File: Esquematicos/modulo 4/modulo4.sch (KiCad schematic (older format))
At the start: 15 parts

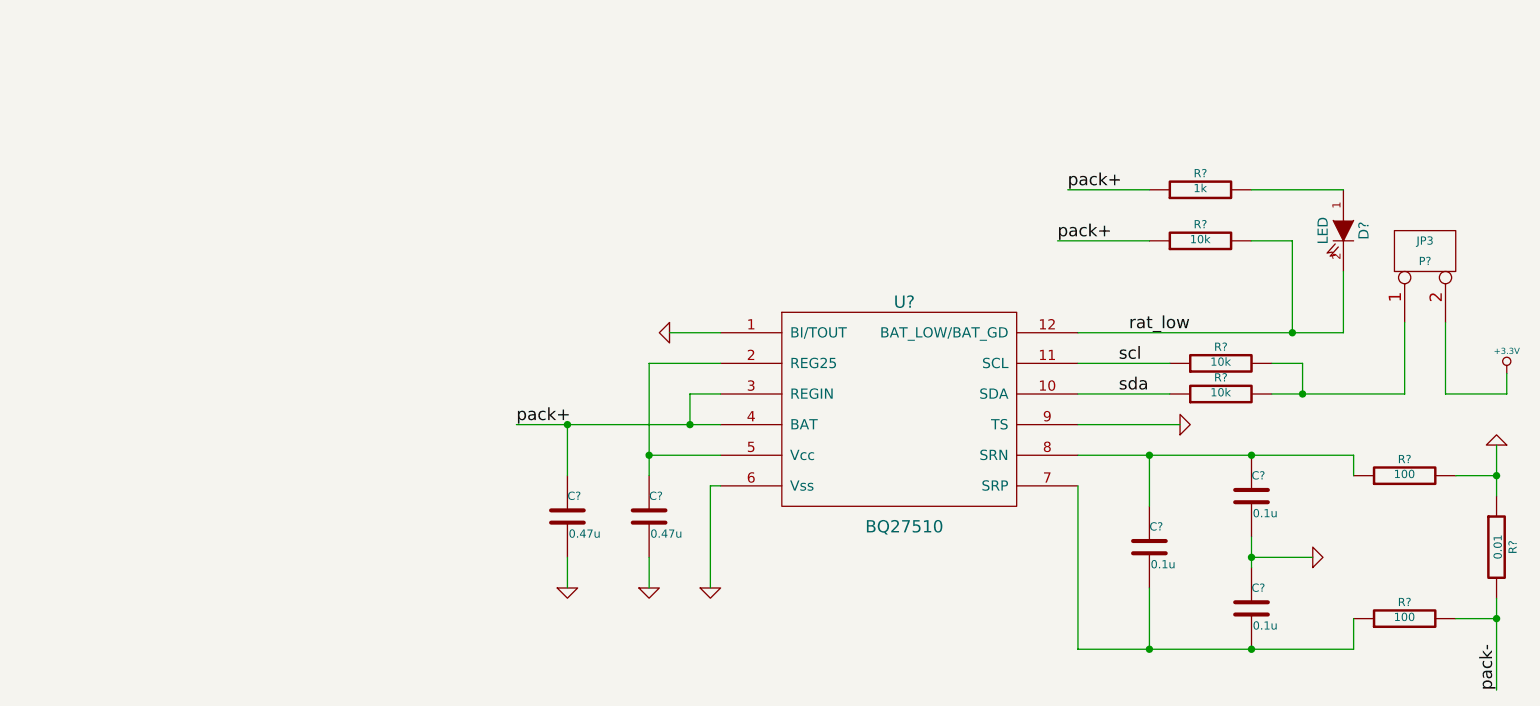
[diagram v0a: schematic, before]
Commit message: cambio modulo
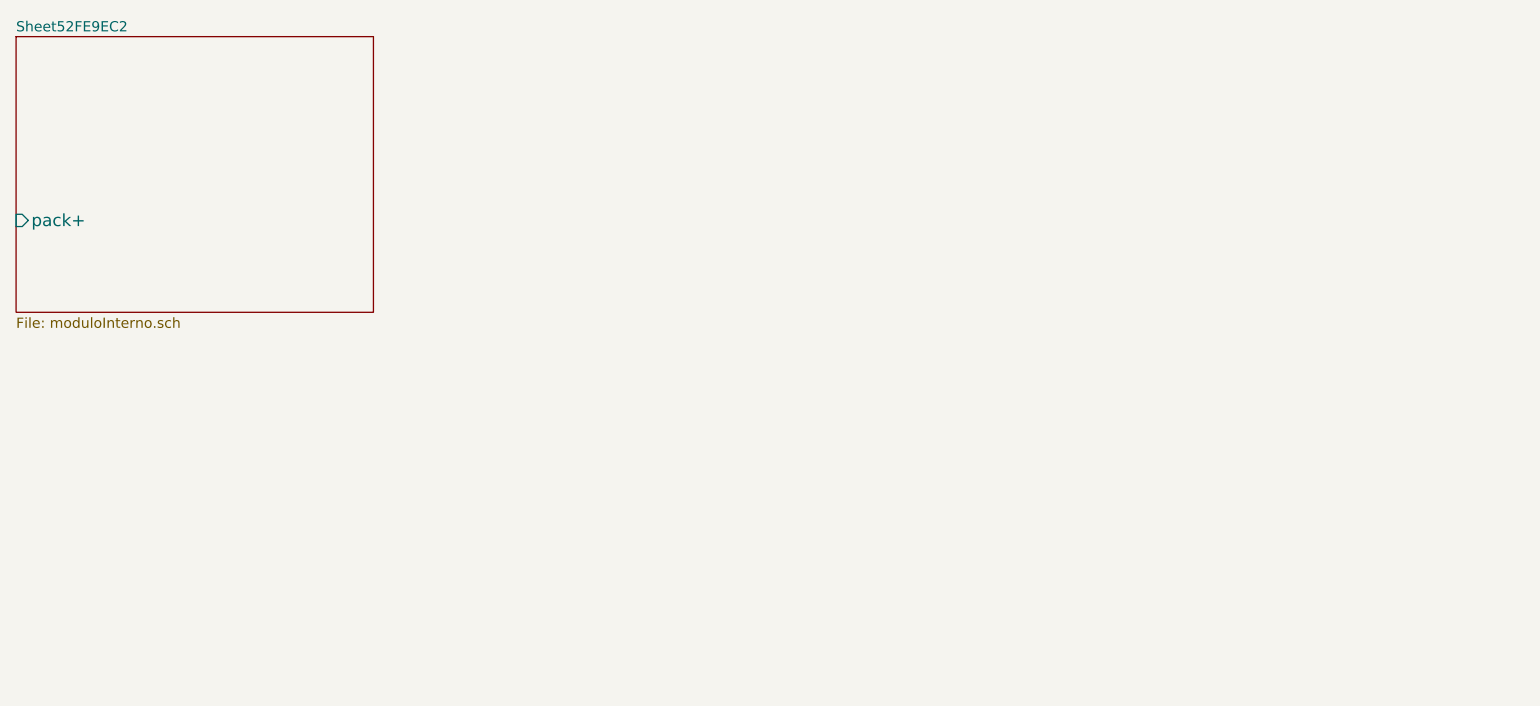
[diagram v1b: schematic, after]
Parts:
- removed C? (x2): 0.47u, ~, symbol C
- removed C? (x3): 0.1u, ~, symbol C
- removed D?: LED, ~, symbol LED
- removed P?: JP3, symbol CONN_2
- removed R? (x3): 10k, ~, symbol R
- removed R?: 1k, ~, symbol R
- removed R? (x2): 100, ~, symbol R
- removed R?: 0.01, ~, symbol R
- removed U?: BQ27510, ~, symbol BQ27510

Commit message: Esquematico terminado
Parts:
- added C? (x4): 10u, ~, symbol C
- added D? (x2): ZENER, ~, symbol ZENER
- added JP? (x2): JUMPER, ~, symbol JUMPER
- added L? (x2): 2.2U, ~, symbol INDUCTOR
- added P?: batt, symbol CONN_2
- added P?: jp1, symbol CONN_20X2
- added P?: jp2, symbol CONN_20X2
- added R? (x3): 0, ~, symbol R
- added R? (x2): 10k, ~, symbol R
- added R? (x2): dnp, ~, symbol R
- added U?: MINI_USB, ~, symbol MINI_USB
- added U?: TPS63001, ~, symbol TPS63001
- added U?: TPS63002, ~, symbol TPS63002
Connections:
- new net: L?.2, U?.2 (L2) (x2)
- new net: L?.1, U?.4 (L1) (x2)
- new net: R?.1, R?.2, U?.7 (PS/SYNC) (x2)
- new net: D?.2 (K), JP?.2 (x2)
- new net: C?.1, D?.1 (A), U?.1 (VOUT), U?.10 (FB)
- new net +3.3V: C?.1, D?.1 (A), U?.1 (VOUT), U?.10 (FB)
- new net +5V: U?.1 (VBUS)
- new net 3.3_charge: JP?.1, P?.1 (P1)
- new net 5_charge: JP?.1, P?.2 (P2)
- new net GND: C?.2, C?.2, C?.2, C?.2, P?.2 (P2), R?.2, R?.2, U?.3 (PGND), U?.3 (PGND), U?.5 (GND), U?.9 (GND), U?.9 (GND)
- new net charge: R?.1
- new net charge_lp: P?.3 (P3), R?.2
- new net en: R?.2
- new net en_lp: P?.9 (P9), R?.1
- new net pack+: C?.1, C?.1, P?.2 (PM), R?.1, R?.1, U?.5 (VIN), U?.5 (VIN), U?.8 (VINA), U?.8 (VINA)
- new net pack-: P?.1 (P1)
- new net pg: R?.2
- new net pg_lp: P?.13 (P13), R?.1
- new net rat_low: U?.6 (EN), U?.6 (EN)
- new net scl: P?.14 (P14)
- new net sda: P?.12 (P12)
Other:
- note added: "BATTERY\n"
- note added: "CHARGE CONECTOR"
- note added: "CHARGE MONITORING"

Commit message: cambios
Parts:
- removed P?: jp1, symbol CONN_20X2
- removed P?: jp2, symbol CONN_20X2
- added P1, P2: CONN_10X2, symbol CONN_10X2
- gave numbers to parts that had none: 21
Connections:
- net 3.3_charge: now also P1.1 (P1)
- net 5_charge: now also P1.2 (P2)
- net GND: now also P2.2 (P2)
- net charge_lp: now also P1.3 (P3)
- net en_lp: now also P1.9 (P9)
- net pg_lp: now also P1.13 (P13)
- net scl: now also P2.14 (P14)
- net sda: now also P2.12 (P12)
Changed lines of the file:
@@
 Sheet 1 3
 Title ""
-Date "18 feb 2014"
+Date "19 feb 2014"
 Rev ""
 Comp ""
@@
 $EndSheet
 $Comp
-L CONN_2 P?
+L CONN_2 P3
 U 1 1 52FF069F
 P 5850 5000
-F 0 "P?" V 5800 5000 40  0000 C CNN
+F 0 "P3" V 5800 5000 40  0000 C CNN
 F 1 "batt" V 5900 5000 40  0000 C CNN
 F 2 "" H 5850 5000 60  0000 C CNN
@@
 $EndComp
 $Comp
-L MINI_USB U?
+L MINI_USB U1
 U 1 1 530190CF
 P 1950 4450
-F 0 "U?" H 1950 4100 60  0000 C CNN
+F 0 "U1" H 1950 4100 60  0000 C CNN
 F 1 "MINI_USB" H 1950 4800 60  0000 C CNN
 F 2 "~" H 1850 4250 60  0000 C CNN
@@
 $EndComp
 $Comp
-L GND #PWR?
+L GND #PWR01
 U 1 1 530191E1
 P 1150 4650
-F 0 "#PWR?" H 1150 4650 30  0001 C CNN
+F 0 "#PWR01" H 1150 4650 30  0001 C CNN
 F 1 "GND" H 1150 4580 30  0001 C CNN
 F 2 "" H 1150 4650 60  0000 C CNN
@@
 $EndComp
 $Comp
-L +5V #PWR?
+L +5V #PWR02
 U 1 1 530191F0
 P 1100 4200
-F 0 "#PWR?" H 1100 4290 20  0001 C CNN
+F 0 "#PWR02" H 1100 4290 20  0001 C CNN
 F 1 "+5V" H 1100 4290 30  0000 C CNN
 F 2 "" H 1100 4200 60  0000 C CNN
@@
 $EndComp
 $Comp
-L R R?
+L R R1
 U 1 1 5302956B
 P 3600 4500
-F 0 "R?" V 3680 4500 40  0000 C CNN
+F 0 "R1" V 3680 4500 40  0000 C CNN
 F 1 "0" V 3607 4501 40  0000 C CNN
 F 2 "~" V 3530 4500 30  0000 C CNN
@@
 $EndComp
 $Comp
-L R R?
+L R R2
 U 1 1 5302957A
 P 4050 4500
-F 0 "R?" V 4130 4500 40  0000 C CNN
+F 0 "R2" V 4130 4500 40  0000 C CNN
 F 1 "0" V 4057 4501 40  0000 C CNN
 F 2 "~" V 3980 4500 30  0000 C CNN
@@
 $EndComp
 $Comp
-L R R?
+L R R3
 U 1 1 53029589
 P 4450 4500
-F 0 "R?" V 4530 4500 40  0000 C CNN
+F 0 "R3" V 4530 4500 40  0000 C CNN
 F 1 "0" V 4457 4501 40  0000 C CNN
 F 2 "~" V 4380 4500 30  0000 C CNN
@@
 pg
 $Comp
-L TPS63001 U?
+L TPS63001 U3
 U 1 1 5302BE15
 P 9250 1650
-F 0 "U?" H 9250 1250 60  0000 C CNN
+F 0 "U3" H 9250 1250 60  0000 C CNN
 F 1 "TPS63001" H 9250 2100 60  0000 C CNN
 F 2 "~" H 9250 1750 60  0000 C CNN
@@
 $EndComp
 $Comp
-L INDUCTOR L?
+L INDUCTOR L2
 U 1 1 5302C133
 P 8150 1700
-F 0 "L?" V 8100 1700 40  0000 C CNN
+F 0 "L2" V 8100 1700 40  0000 C CNN
 F 1 "2.2U" V 8250 1700 40  0000 C CNN
 F 2 "~" H 8150 1700 60  0000 C CNN
@@
 pack+
 $Comp
-L C C?
+L C C4
 U 1 1 5302C501
 P 8550 2550
-F 0 "C?" H 8550 2650 40  0000 L CNN
+F 0 "C4" H 8550 2650 40  0000 L CNN
 F 1 "10u" H 8556 2465 40  0000 L CNN
 F 2 "~" H 8588 2400 30  0000 C CNN
@@
 $EndComp
 $Comp
-L GND #PWR?
+L GND #PWR03
 U 1 1 5302C5BE
 P 8550 2850
-F 0 "#PWR?" H 8550 2850 30  0001 C CNN
+F 0 "#PWR03" H 8550 2850 30  0001 C CNN
 F 1 "GND" H 8550 2780 30  0001 C CNN
 F 2 "" H 8550 2850 60  0000 C CNN
@@
 rat_low
 $Comp
-L R R?
+L R R6
 U 1 1 5302CB80
 P 10050 2600
-F 0 "R?" V 10130 2600 40  0000 C CNN
+F 0 "R6" V 10130 2600 40  0000 C CNN
 F 1 "10k" V 10057 2601 40  0000 C CNN
 F 2 "~" V 9980 2600 30  0000 C CNN
@@
 $EndComp
 $Comp
-L R R?
+L R R7
 U 1 1 5302CCF8
 P 10050 3350
-F 0 "R?" V 10130 3350 40  0000 C CNN
+F 0 "R7" V 10130 3350 40  0000 C CNN
 F 1 "dnp" V 10057 3351 40  0000 C CNN
 F 2 "~" V 9980 3350 30  0000 C CNN
@@
 $EndComp
 $Comp
-L GND #PWR?
+L GND #PWR04
 U 1 1 5302CD88
 P 10050 3700
-F 0 "#PWR?" H 10050 3700 30  0001 C CNN
+F 0 "#PWR04" H 10050 3700 30  0001 C CNN
 F 1 "GND" H 10050 3630 30  0001 C CNN
 F 2 "" H 10050 3700 60  0000 C CNN
@@
 $EndComp
 $Comp
-L GND #PWR?
+L GND #PWR05
 U 1 1 5302CEF5
 P 9300 900
-F 0 "#PWR?" H 9300 900 30  0001 C CNN
+F 0 "#PWR05" H 9300 900 30  0001 C CNN
 F 1 "GND" H 9300 830 30  0001 C CNN
 F 2 "" H 9300 900 60  0000 C CNN
@@
 $EndComp
 $Comp
-L C C?
+L C C2
 U 1 1 5302CFFE
 P 7850 1250
-F 0 "C?" H 7850 1350 40  0000 L CNN
+F 0 "C2" H 7850 1350 40  0000 L CNN
 F 1 "10u" H 7856 1165 40  0000 L CNN
 F 2 "~" H 7888 1100 30  0000 C CNN
@@
 $EndComp
 $Comp
-L GND #PWR?
+L GND #PWR06
 U 1 1 5302D066
 P 7850 1600
-F 0 "#PWR?" H 7850 1600 30  0001 C CNN
+F 0 "#PWR06" H 7850 1600 30  0001 C CNN
 F 1 "GND" H 7850 1530 30  0001 C CNN
 F 2 "" H 7850 1600 60  0000 C CNN
@@
 $EndComp
 $Comp
-L ZENER D?
+L ZENER D2
 U 1 1 5302D119
 P 7500 1000
-F 0 "D?" H 7500 1100 50  0000 C CNN
+F 0 "D2" H 7500 1100 50  0000 C CNN
 F 1 "ZENER" H 7500 900 40  0000 C CNN
 F 2 "~" H 7500 1000 60  0000 C CNN
@@
 $EndComp
 $Comp
-L +3.3V #PWR?
+L +3.3V #PWR07
 U 1 1 5302D183
 P 8050 850
-F 0 "#PWR?" H 8050 810 30  0001 C CNN
+F 0 "#PWR07" H 8050 810 30  0001 C CNN
 F 1 "+3.3V" H 8050 960 30  0000 C CNN
 F 2 "" H 8050 850 60  0000 C CNN
@@
 $EndComp
 $Comp
-L JUMPER JP?
+L JUMPER JP2
 U 1 1 5302D317
 P 7150 1450
-F 0 "JP?" H 7150 1600 60  0000 C CNN
+F 0 "JP2" H 7150 1600 60  0000 C CNN
 F 1 "JUMPER" H 7150 1370 40  0000 C CNN
 F 2 "~" H 7150 1450 60  0000 C CNN
@@
 3.3_charge
 $Comp
-L INDUCTOR L?
+L INDUCTOR L1
 U 1 1 5302D7F1
 P 8100 4950
-F 0 "L?" V 8050 4950 40  0000 C CNN
+F 0 "L1" V 8050 4950 40  0000 C CNN
 F 1 "2.2U" V 8200 4950 40  0000 C CNN
 F 2 "~" H 8100 4950 60  0000 C CNN
@@
 pack+
 $Comp
-L C C?
+L C C3
 U 1 1 5302D7F8
 P 8500 5800
-F 0 "C?" H 8500 5900 40  0000 L CNN
+F 0 "C3" H 8500 5900 40  0000 L CNN
 F 1 "10u" H 8506 5715 40  0000 L CNN
 F 2 "~" H 8538 5650 30  0000 C CNN
@@
 $EndComp
 $Comp
-L GND #PWR?
+L GND #PWR08
 U 1 1 5302D7FE
 P 8500 6100
-F 0 "#PWR?" H 8500 6100 30  0001 C CNN
+F 0 "#PWR08" H 8500 6100 30  0001 C CNN
 F 1 "GND" H 8500 6030 30  0001 C CNN
 F 2 "" H 8500 6100 60  0000 C CNN
@@
 rat_low
 $Comp
-L R R?
+L R R4
 U 1 1 5302D805
 P 10000 5850
-F 0 "R?" V 10080 5850 40  0000 C CNN
+F 0 "R4" V 10080 5850 40  0000 C CNN
 F 1 "10k" V 10007 5851 40  0000 C CNN
 F 2 "~" V 9930 5850 30  0000 C CNN
@@
 $EndComp
 $Comp
-L R R?
+L R R5
 U 1 1 5302D80B
 P 10000 6600
-F 0 "R?" V 10080 6600 40  0000 C CNN
+F 0 "R5" V 10080 6600 40  0000 C CNN
 F 1 "dnp" V 10007 6601 40  0000 C CNN
 F 2 "~" V 9930 6600 30  0000 C CNN
@@
 $EndComp
 $Comp
-L GND #PWR?
+L GND #PWR09
 U 1 1 5302D811
 P 10000 6950
-F 0 "#PWR?" H 10000 6950 30  0001 C CNN
+F 0 "#PWR09" H 10000 6950 30  0001 C CNN
 F 1 "GND" H 10000 6880 30  0001 C CNN
 F 2 "" H 10000 6950 60  0000 C CNN
@@
 $EndComp
 $Comp
-L GND #PWR?
+L GND #PWR010
 U 1 1 5302D817
 P 9250 4150
-F 0 "#PWR?" H 9250 4150 30  0001 C CNN
+F 0 "#PWR010" H 9250 4150 30  0001 C CNN
 F 1 "GND" H 9250 4080 30  0001 C CNN
 F 2 "" H 9250 4150 60  0000 C CNN
@@
 $EndComp
 $Comp
-L C C?
+L C C1
 U 1 1 5302D81D
 P 7800 4500
-F 0 "C?" H 7800 4600 40  0000 L CNN
+F 0 "C1" H 7800 4600 40  0000 L CNN
 F 1 "10u" H 7806 4415 40  0000 L CNN
 F 2 "~" H 7838 4350 30  0000 C CNN
@@
 $EndComp
 $Comp
-L GND #PWR?
+L GND #PWR011
 U 1 1 5302D823
 P 7800 4850
-F 0 "#PWR?" H 7800 4850 30  0001 C CNN
+F 0 "#PWR011" H 7800 4850 30  0001 C CNN
 F 1 "GND" H 7800 4780 30  0001 C CNN
 F 2 "" H 7800 4850 60  0000 C CNN
@@
 $EndComp
 $Comp
-L ZENER D?
+L ZENER D1
 U 1 1 5302D829
 P 7450 4250
-F 0 "D?" H 7450 4350 50  0000 C CNN
+F 0 "D1" H 7450 4350 50  0000 C CNN
 F 1 "ZENER" H 7450 4150 40  0000 C CNN
 F 2 "~" H 7450 4250 60  0000 C CNN
@@
 $EndComp
 $Comp
-L JUMPER JP?
+L JUMPER JP1
 U 1 1 5302D835
 P 7100 4700
-F 0 "JP?" H 7100 4850 60  0000 C CNN
+F 0 "JP1" H 7100 4850 60  0000 C CNN
 F 1 "JUMPER" H 7100 4620 40  0000 C CNN
 F 2 "~" H 7100 4700 60  0000 C CNN
@@
 5_charge
 $Comp
-L TPS63002 U?
+L TPS63002 U2
 U 1 1 5302DB33
 P 9200 4900
-F 0 "U?" H 9200 4450 60  0000 C CNN
+F 0 "U2" H 9200 4450 60  0000 C CNN
 F 1 "TPS63002" H 9200 5350 60  0000 C CNN
 F 2 "~" H 9300 4850 60  0000 C CNN
@@
 	1    9200 4900
 	1    0    0    -1
-$EndComp
-$Comp
-L CONN_20X2 P?
-U 1 1 5302E1CD
-P 2450 6800
-F 0 "P?" H 2450 7850 60  0000 C CNN
-F 1 "jp1" V 2450 6800 50  0000 C CNN
-F 2 "" H 2450 6800 60  0000 C CNN
-F 3 "" H 2450 6800 60  0000 C CNN
-	1    2450 6800
-	0    -1   -1   0
-$EndComp
-$Comp
-L CONN_20X2 P?
-U 1 1 5302E1DA
-P 5450 6850
-F 0 "P?" H 5450 7900 60  0000 C CNN
-F 1 "jp2" V 5450 6850 50  0000 C CNN
-F 2 "" H 5450 6850 60  0000 C CNN
-F 3 "" H 5450 6850 60  0000 C CNN
-	1    5450 6850
-	0    -1   -1   0
 $EndComp
 Wire Wire Line
@@
 	4500 6450 4500 6150
 $Comp
-L GND #PWR?
+L GND #PWR012
 U 1 1 5302F4ED
 P 4500 6150
-F 0 "#PWR?" H 4500 6150 30  0001 C CNN
+F 0 "#PWR012" H 4500 6150 30  0001 C CNN
 F 1 "GND" H 4500 6080 30  0001 C CNN
 F 2 "" H 4500 6150 60  0000 C CNN
@@
 Wire Wire Line
 	1200 2350 600  2350
+$Comp
+L CONN_10X2 P1
+U 1 1 53040A04
+P 1950 6800
+F 0 "P1" H 1950 7350 60  0000 C CNN
+F 1 "CONN_10X2" V 1950 6700 50  0000 C CNN
+F 2 "" H 1950 6800 60  0000 C CNN
+F 3 "" H 1950 6800 60  0000 C CNN
+	1    1950 6800
+	0    -1   -1   0
+$EndComp
+$Comp
+L CONN_10X2 P2
+U 1 1 53040B6B
+P 4950 6850
+F 0 "P2" H 4950 7400 60  0000 C CNN
+F 1 "CONN_10X2" V 4950 6750 50  0000 C CNN
+F 2 "" H 4950 6850 60  0000 C CNN
+F 3 "" H 4950 6850 60  0000 C CNN
+	1    4950 6850
+	0    -1   -1   0
+$EndComp
 $EndSCHEMATC

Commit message: recuperacion
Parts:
- removed C1, C2, C3, C4: 10u, ~, symbol C
- removed D1, D2: ZENER, ~, symbol ZENER
- removed JP1, JP2: JUMPER, ~, symbol JUMPER
- removed L1, L2: 2.2U, ~, symbol INDUCTOR
- removed P1, P2: CONN_10X2, symbol CONN_10X2
- removed P3: batt, symbol CONN_2
- removed R1, R2, R3: 0, ~, symbol R
- removed R4, R6: 10k, ~, symbol R
- removed R5, R7: dnp, ~, symbol R
- removed U1: MINI_USB, ~, symbol MINI_USB
- removed U2: TPS63002, ~, symbol TPS63002
- removed U3: TPS63001, ~, symbol TPS63001
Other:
- note removed: "BATTERY\n"
- note removed: "CHARGE CONECTOR"
- note removed: "CHARGE MONITORING"
